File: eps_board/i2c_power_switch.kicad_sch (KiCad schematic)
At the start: 6 parts, among them U29 MCP23008T-E/SS

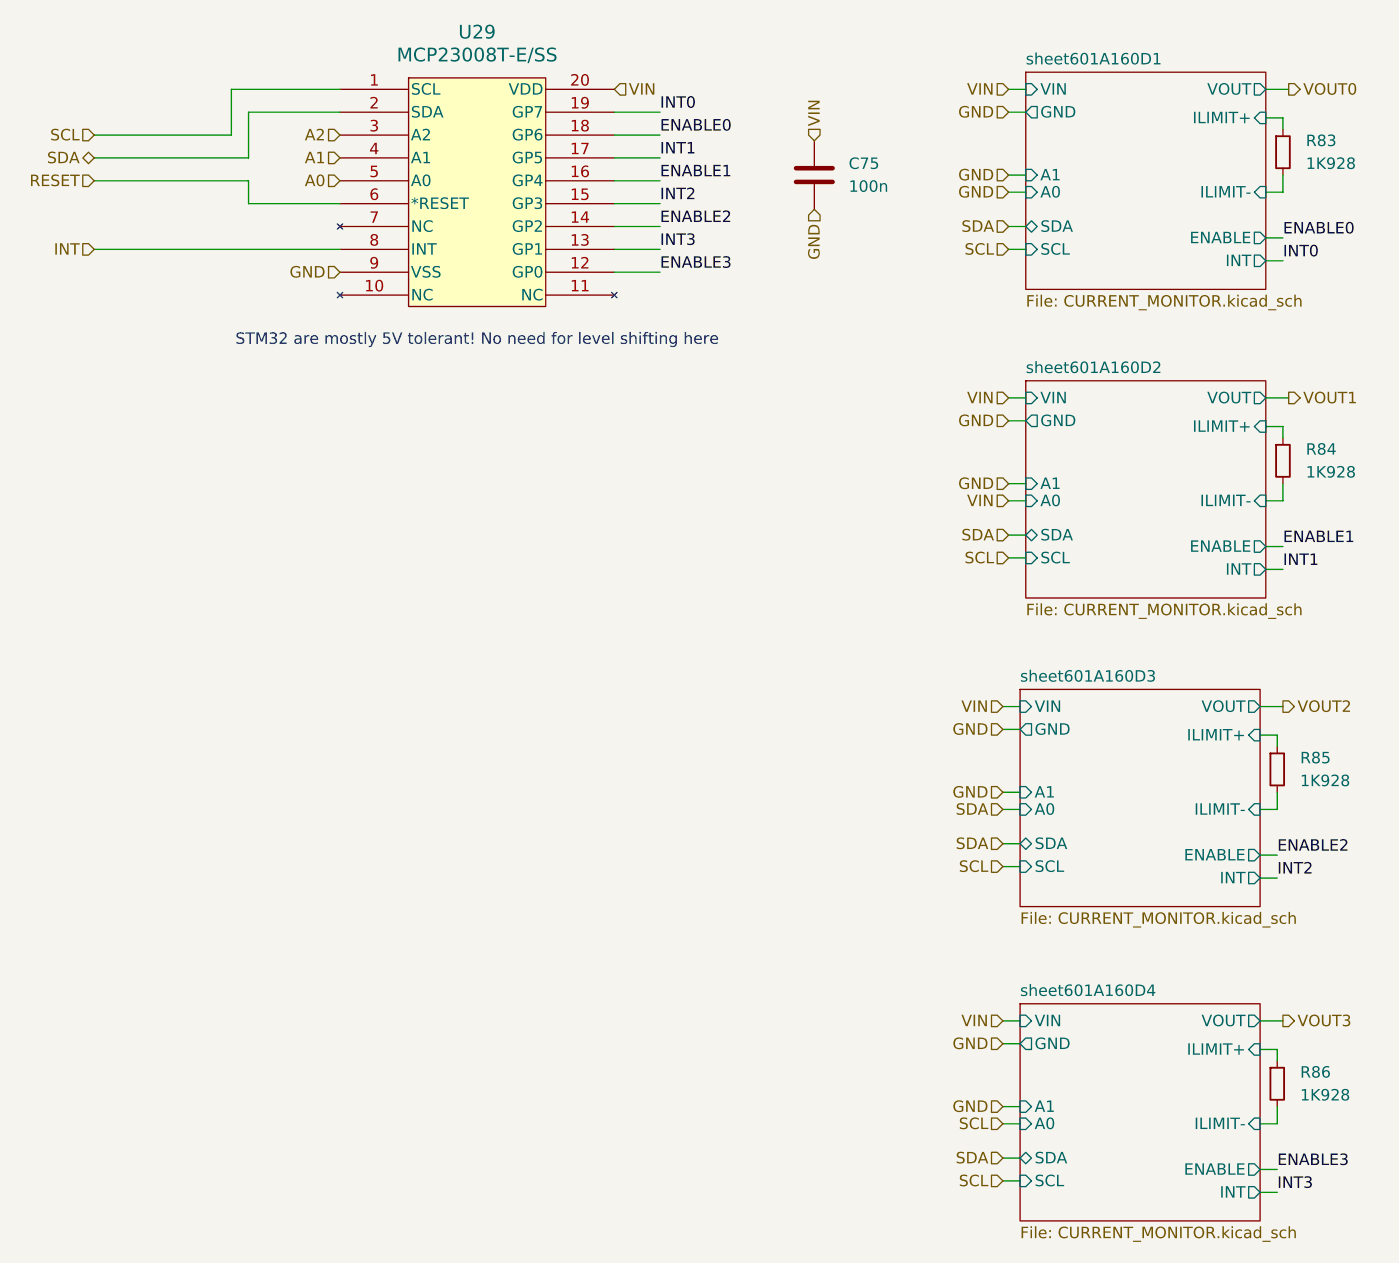
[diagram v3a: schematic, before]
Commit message: light sensors with i2c multiplexers for AVI board. i2c amp/volt meter for attitude control coils
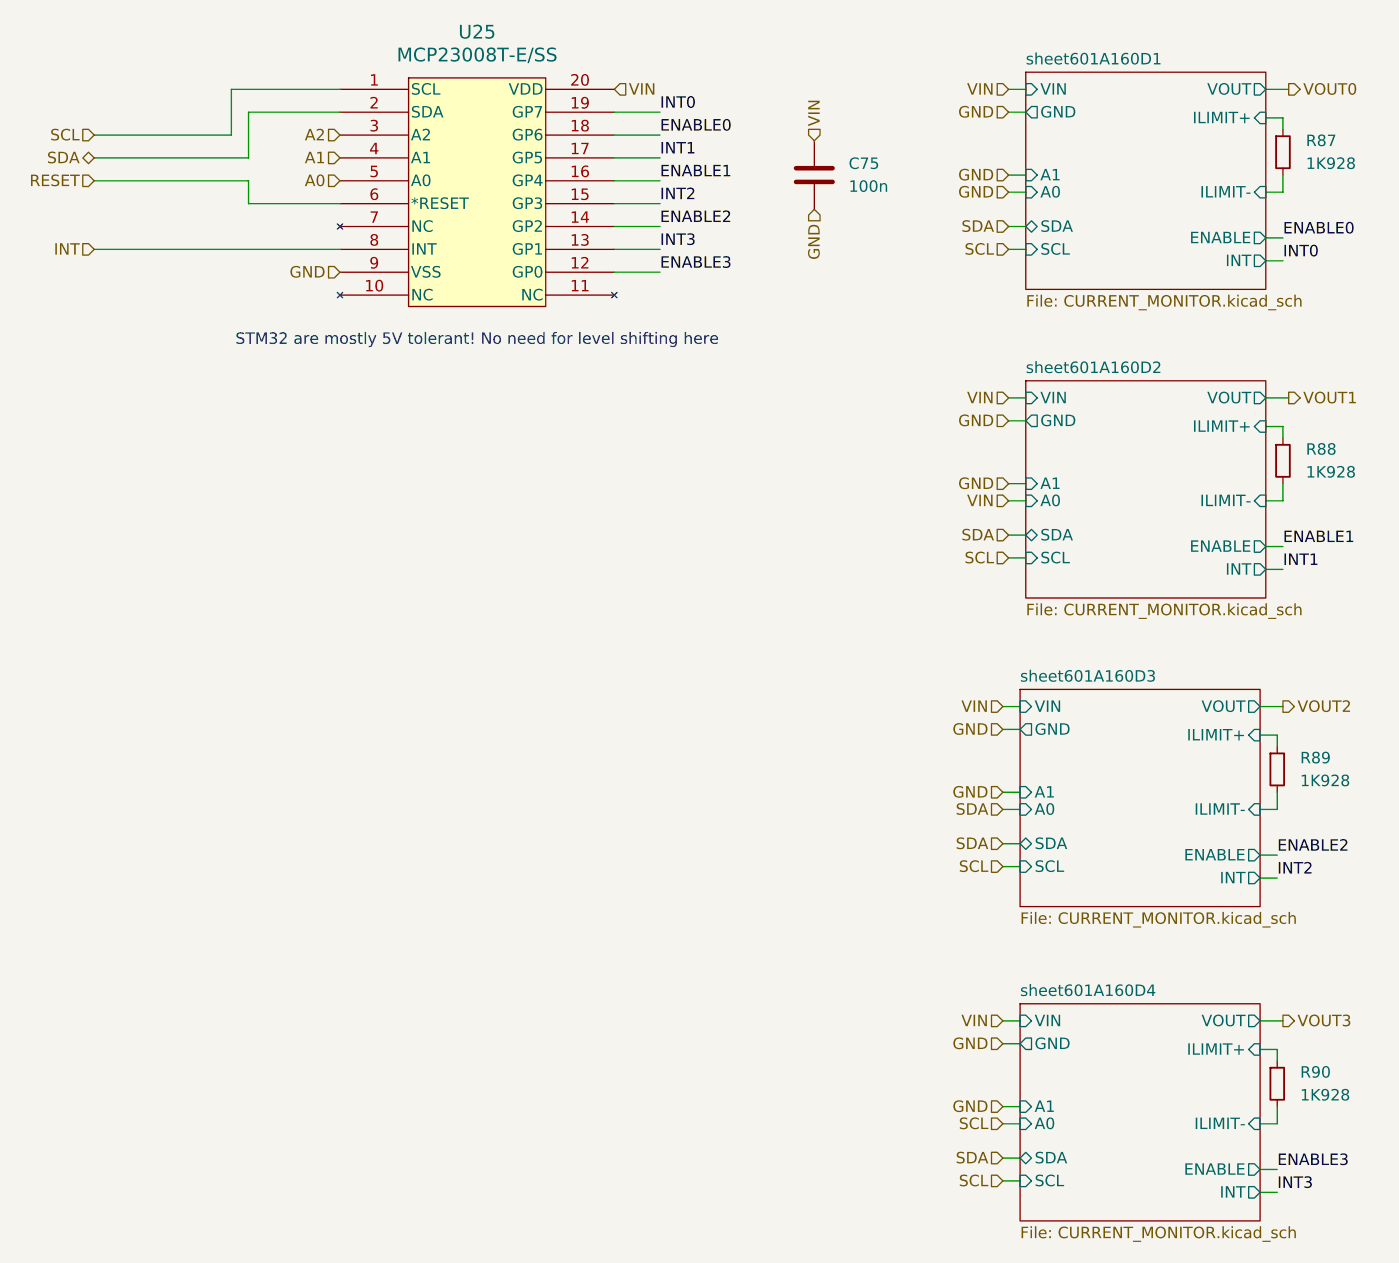
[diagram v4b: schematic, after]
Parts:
- renumbered R83 to R87, R84 to R88, R85 to R89, R86 to R90, U29 to U25
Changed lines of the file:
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@@
 		(dnp no)
 		(fields_autoplaced yes)
-		(property "Reference" "R84"
+		(property "Reference" "R88"
 			(at 172.085 71.7549 0)
 			(effects
@@
 			(project "EPS"
 				(path "/05170af6-30ef-4c3a-b972-f098085da1bc/53211e67-c677-4be8-893d-9825fa308902"
-					(reference "R84")
+					(reference "R88")
 					(unit 1)
 				)
@@
 		(dnp no)
 		(fields_autoplaced yes)
-		(property "Reference" "R86"
+		(property "Reference" "R90"
 			(at 171.45 140.9699 0)
 			(effects
@@
 			(project "EPS"
 				(path "/05170af6-30ef-4c3a-b972-f098085da1bc/53211e67-c677-4be8-893d-9825fa308902"
-					(reference "R86")
+					(reference "R90")
 					(unit 1)
 				)
@@
 		(dnp no)
 		(fields_autoplaced yes)
-		(property "Reference" "R83"
+		(property "Reference" "R87"
 			(at 172.085 37.4649 0)
 			(effects
@@
 			(project "EPS"
 				(path "/05170af6-30ef-4c3a-b972-f098085da1bc/53211e67-c677-4be8-893d-9825fa308902"
-					(reference "R83")
+					(reference "R87")
 					(unit 1)
 				)
@@
 		(dnp no)
 		(fields_autoplaced yes)
-		(property "Reference" "R85"
+		(property "Reference" "R89"
 			(at 171.45 106.0449 0)
 			(effects
@@
 			(project "EPS"
 				(path "/05170af6-30ef-4c3a-b972-f098085da1bc/53211e67-c677-4be8-893d-9825fa308902"
-					(reference "R85")
+					(reference "R89")
 					(unit 1)
 				)
@@
 		(dnp no)
 		(fields_autoplaced yes)
-		(property "Reference" "U29"
+		(property "Reference" "U25"
 			(at 80.01 25.4 0)
 			(effects
@@
 			(project ""
 				(path "/05170af6-30ef-4c3a-b972-f098085da1bc/53211e67-c677-4be8-893d-9825fa308902"
-					(reference "U29")
-					(unit 1)
-				)
+					(reference "U25")
+					(unit 1)
+				)

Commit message: interim checkin for EPS BOM
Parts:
- C75: value 100n -> 100nF; Manufacturer (none) -> Murata; Part Number (none) -> GRM155R61E104KA87D; Tolerance (none) -> 10; Voltage (none) -> 25
- R87, R88, R89, R90: footprint Resistor_SMD:R_0603_1608Metric_Pad0.98x0.95mm_HandSolder -> Resistor_SMD:R_0402_1005Metric_Pad0.72x0.64mm_HandSolder; Manufacturer (none) -> YAGEO; Part Number (none) -> RC0402FR-071K928L; Tolerance (none) -> 1
- U25: symbol Project:MCP23008T-E_SS -> Common:MCP23008T-E_SS
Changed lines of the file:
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@@
 			)
 		)
-		(property "Value" "100n"
+		(property "Value" "100nF"
 			(at 121.285 42.5449 0)
 			(effects
@@
 			)
 		)
-		(property "Datasheet" "~"
+		(property "Datasheet" "https://search.murata.co.jp/Ceramy/image/img/A01X/G101/ENG/GRM155R61E104KA87-01.pdf"
 			(at 117.475 41.275 0)
 			(effects
@@
 		)
 		(property "Description" "Unpolarized capacitor"
+			(at 117.475 41.275 0)
+			(effects
+				(font
+					(size 1.27 1.27)
+				)
+				(hide yes)
+			)
+		)
+		(property "Manufacturer" "Murata"
+			(at 117.475 41.275 0)
+			(effects
+				(font
+					(size 1.27 1.27)
+				)
+				(hide yes)
+			)
+		)
+		(property "Part Number" "GRM155R61E104KA87D"
+			(at 117.475 41.275 0)
+			(effects
+				(font
+					(size 1.27 1.27)
+				)
+				(hide yes)
+			)
+		)
+		(property "Voltage" "25"
+			(at 117.475 41.275 0)
+			(effects
+				(font
+					(size 1.27 1.27)
+				)
+				(hide yes)
+			)
+		)
+		(property "Tolerance" "10"
 			(at 117.475 41.275 0)
 			(effects
@@
 			)
 		)
-		(property "Footprint" "Resistor_SMD:R_0603_1608Metric_Pad0.98x0.95mm_HandSolder"
-			(at 169.545 73.025 0)
-			(effects
-				(font
-					(size 1.27 1.27)
-				)
-				(hide yes)
-			)
-		)
-		(property "Datasheet" "~"
+		(property "Footprint" "Resistor_SMD:R_0402_1005Metric_Pad0.72x0.64mm_HandSolder"
+			(at 169.545 73.025 0)
+			(effects
+				(font
+					(size 1.27 1.27)
+				)
+				(hide yes)
+			)
+		)
+		(property "Datasheet" "https://www.yageo.com/upload/media/product/products/datasheet/rchip/PYu-RC_Group_51_RoHS_L_12.pdf"
 			(at 169.545 73.025 0)
 			(effects
@@
 		)
 		(property "Description" "Resistor, small symbol"
+			(at 169.545 73.025 0)
+			(effects
+				(font
+					(size 1.27 1.27)
+				)
+				(hide yes)
+			)
+		)
+		(property "Manufacturer" "YAGEO"
+			(at 169.545 73.025 0)
+			(effects
+				(font
+					(size 1.27 1.27)
+				)
+				(hide yes)
+			)
+		)
+		(property "Part Number" "RC0402FR-071K928L"
+			(at 169.545 73.025 0)
+			(effects
+				(font
+					(size 1.27 1.27)
+				)
+				(hide yes)
+			)
+		)
+		(property "Tolerance" "1"
 			(at 169.545 73.025 0)
 			(effects
@@
 			)
 		)
-		(property "Footprint" "Resistor_SMD:R_0603_1608Metric_Pad0.98x0.95mm_HandSolder"
-			(at 168.91 142.24 0)
-			(effects
-				(font
-					(size 1.27 1.27)
-				)
-				(hide yes)
-			)
-		)
-		(property "Datasheet" "~"
+		(property "Footprint" "Resistor_SMD:R_0402_1005Metric_Pad0.72x0.64mm_HandSolder"
+			(at 168.91 142.24 0)
+			(effects
+				(font
+					(size 1.27 1.27)
+				)
+				(hide yes)
+			)
+		)
+		(property "Datasheet" "https://www.yageo.com/upload/media/product/products/datasheet/rchip/PYu-RC_Group_51_RoHS_L_12.pdf"
 			(at 168.91 142.24 0)
 			(effects
@@
 		)
 		(property "Description" "Resistor, small symbol"
+			(at 168.91 142.24 0)
+			(effects
+				(font
+					(size 1.27 1.27)
+				)
+				(hide yes)
+			)
+		)
+		(property "Manufacturer" "YAGEO"
+			(at 168.91 142.24 0)
+			(effects
+				(font
+					(size 1.27 1.27)
+				)
+				(hide yes)
+			)
+		)
+		(property "Part Number" "RC0402FR-071K928L"
+			(at 168.91 142.24 0)
+			(effects
+				(font
+					(size 1.27 1.27)
+				)
+				(hide yes)
+			)
+		)
+		(property "Tolerance" "1"
 			(at 168.91 142.24 0)
 			(effects
@@
 			)
 		)
-		(property "Footprint" "Resistor_SMD:R_0603_1608Metric_Pad0.98x0.95mm_HandSolder"
-			(at 169.545 38.735 0)
-			(effects
-				(font
-					(size 1.27 1.27)
-				)
-				(hide yes)
-			)
-		)
-		(property "Datasheet" "~"
+		(property "Footprint" "Resistor_SMD:R_0402_1005Metric_Pad0.72x0.64mm_HandSolder"
+			(at 169.545 38.735 0)
+			(effects
+				(font
+					(size 1.27 1.27)
+				)
+				(hide yes)
+			)
+		)
+		(property "Datasheet" "https://www.yageo.com/upload/media/product/products/datasheet/rchip/PYu-RC_Group_51_RoHS_L_12.pdf"
 			(at 169.545 38.735 0)
 			(effects
@@
 		)
 		(property "Description" "Resistor, small symbol"
+			(at 169.545 38.735 0)
+			(effects
+				(font
+					(size 1.27 1.27)
+				)
+				(hide yes)
+			)
+		)
+		(property "Manufacturer" "YAGEO"
+			(at 169.545 38.735 0)
+			(effects
+				(font
+					(size 1.27 1.27)
+				)
+				(hide yes)
+			)
+		)
+		(property "Part Number" "RC0402FR-071K928L"
+			(at 169.545 38.735 0)
+			(effects
+				(font
+					(size 1.27 1.27)
+				)
+				(hide yes)
+			)
+		)
+		(property "Tolerance" "1"
 			(at 169.545 38.735 0)
 			(effects
@@
 			)
 		)
-		(property "Footprint" "Resistor_SMD:R_0603_1608Metric_Pad0.98x0.95mm_HandSolder"
-			(at 168.91 107.315 0)
-			(effects
-				(font
-					(size 1.27 1.27)
-				)
-				(hide yes)
-			)
-		)
-		(property "Datasheet" "~"
+		(property "Footprint" "Resistor_SMD:R_0402_1005Metric_Pad0.72x0.64mm_HandSolder"
+			(at 168.91 107.315 0)
+			(effects
+				(font
+					(size 1.27 1.27)
+				)
+				(hide yes)
+			)
+		)
+		(property "Datasheet" "https://www.yageo.com/upload/media/product/products/datasheet/rchip/PYu-RC_Group_51_RoHS_L_12.pdf"
 			(at 168.91 107.315 0)
 			(effects
@@
 		)
 		(property "Description" "Resistor, small symbol"
+			(at 168.91 107.315 0)
+			(effects
+				(font
+					(size 1.27 1.27)
+				)
+				(hide yes)
+			)
+		)
+		(property "Manufacturer" "YAGEO"
+			(at 168.91 107.315 0)
+			(effects
+				(font
+					(size 1.27 1.27)
+				)
+				(hide yes)
+			)
+		)
+		(property "Part Number" "RC0402FR-071K928L"
+			(at 168.91 107.315 0)
+			(effects
+				(font
+					(size 1.27 1.27)
+				)
+				(hide yes)
+			)
+		)
+		(property "Tolerance" "1"
 			(at 168.91 107.315 0)
 			(effects
@@
 	)
 	(symbol
-		(lib_id "Project:MCP23008T-E_SS")
+		(lib_id "Common:MCP23008T-E_SS")
 		(at 57.15 31.75 0)
 		(unit 1)

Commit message: complete BOM assignment for EPS, next step circular check and deep dives
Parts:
- U25: Manufacturer (none) -> Microchip; Part Number (none) -> MCP23008T-E/SS
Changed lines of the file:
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@@
 			)
 		)
-		(property "Datasheet" "MCP23008T-E/SS"
+		(property "Datasheet" "https://ww1.microchip.com/downloads/en/DeviceDoc/MCP23008-MCP23S08-Data-Sheet-20001919F.pdf"
 			(at 64.77 31.75 0)
 			(effects
@@
 			(effects
 				(font
+					(size 1.27 1.27)
+				)
+				(hide yes)
+			)
+		)
+		(property "Manufacturer" "Microchip"
+			(at 57.15 31.75 0)
+			(effects
+				(font
+					(size 1.27 1.27)
+				)
+				(hide yes)
+			)
+		)
+		(property "Part Number" "MCP23008T-E/SS"
+			(at 57.15 31.75 0)
+			(effects
+				(font

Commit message: add decorations and labels to PCBs part 2
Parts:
- R87, R88, R89, R90: footprint Resistor_SMD:R_0402_1005Metric_Pad0.72x0.64mm_HandSolder -> Resistor_SMD:R_0603_1608Metric_Pad0.98x0.95mm_HandSolder; Part Number RC0402FR-071K928L -> RC0603FR-071K928L
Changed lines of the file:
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@@
 			)
 		)
-		(property "Footprint" "Resistor_SMD:R_0402_1005Metric_Pad0.72x0.64mm_HandSolder"
+		(property "Footprint" "Resistor_SMD:R_0603_1608Metric_Pad0.98x0.95mm_HandSolder"
 			(at 169.545 73.025 0)
 			(effects
@@
 			)
 		)
-		(property "Part Number" "RC0402FR-071K928L"
+		(property "Part Number" "RC0603FR-071K928L"
 			(at 169.545 73.025 0)
 			(effects
@@
 			)
 		)
-		(property "Footprint" "Resistor_SMD:R_0402_1005Metric_Pad0.72x0.64mm_HandSolder"
+		(property "Footprint" "Resistor_SMD:R_0603_1608Metric_Pad0.98x0.95mm_HandSolder"
 			(at 168.91 142.24 0)
 			(effects
@@
 			)
 		)
-		(property "Part Number" "RC0402FR-071K928L"
+		(property "Part Number" "RC0603FR-071K928L"
 			(at 168.91 142.24 0)
 			(effects
@@
 			)
 		)
-		(property "Footprint" "Resistor_SMD:R_0402_1005Metric_Pad0.72x0.64mm_HandSolder"
+		(property "Footprint" "Resistor_SMD:R_0603_1608Metric_Pad0.98x0.95mm_HandSolder"
 			(at 169.545 38.735 0)
 			(effects
@@
 			)
 		)
-		(property "Part Number" "RC0402FR-071K928L"
+		(property "Part Number" "RC0603FR-071K928L"
 			(at 169.545 38.735 0)
 			(effects
@@
 			)
 		)
-		(property "Footprint" "Resistor_SMD:R_0402_1005Metric_Pad0.72x0.64mm_HandSolder"
+		(property "Footprint" "Resistor_SMD:R_0603_1608Metric_Pad0.98x0.95mm_HandSolder"
 			(at 168.91 107.315 0)
 			(effects
@@
 			)
 		)
-		(property "Part Number" "RC0402FR-071K928L"
-			(at 168.91 107.315 0)
-			(effects
+		(property "Part Number" "RC0603FR-071K928L"
+			(at 168.91 107.315 0)
+			(effects
